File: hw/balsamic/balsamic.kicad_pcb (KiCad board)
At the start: 2 copper layers, 18.7 x 14.5 mm, 45 parts, among them J1 Conn_01x24, J2 AXT524124, J3 USB_B_Mini, SW1 SW_Push, U1 ISP1807-LR-RS, U2 BMI160, U4 MAX77658AANX+

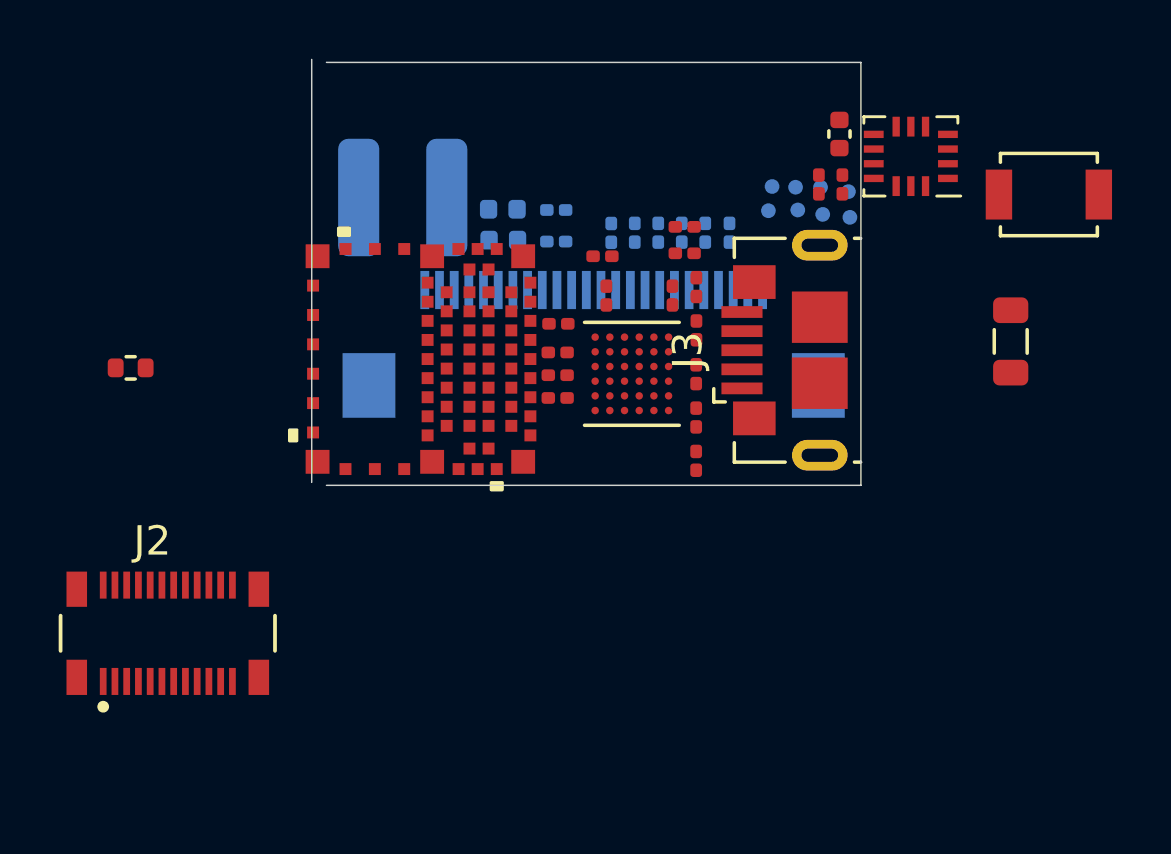
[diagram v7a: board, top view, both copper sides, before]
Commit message: Got board size to 16.1x9.825mm
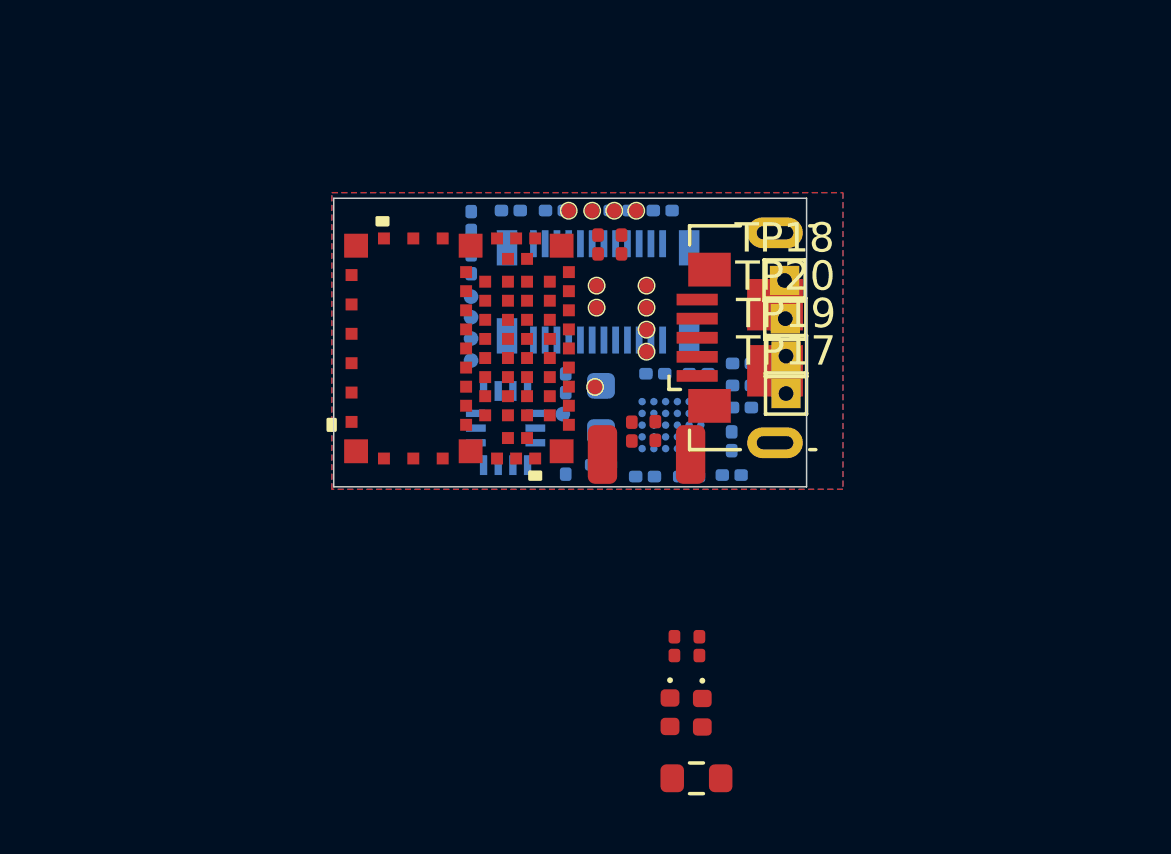
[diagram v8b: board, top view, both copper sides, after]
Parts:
- removed C16, C36: 22uF, Capacitor_SMD:C_0201_0603Metric
- removed C23, C28, C53: 1uF, Capacitor_SMD:C_0201_0603Metric
- removed C34: 10nF, Capacitor_SMD:C_0201_0603Metric
- removed C39: 0.47uF, Capacitor_SMD:C_0201_0603Metric
- removed C46: 100nF, Capacitor_SMD:C_0402_1005Metric
- removed J2: AXT524124, footprints:PANASONIC_AXT524124
- removed L1: 1.5uH, Inductor_SMD:L_0805_2012Metric
- removed R10: 0, Resistor_SMD:R_0201_0603Metric
- removed R11, R12: 4.7K, Resistor_SMD:R_0201_0603Metric
- removed R35: 0, Resistor_SMD:R_0402_1005Metric
- removed R9: 100k, Resistor_SMD:R_0201_0603Metric
- removed U4: MAX77658AANX+, footprints:MAX77658AANX&plus_
- added C1: 22uF, Capacitor_SMD:C_0201_0603Metric, B.Cu at (76.5, 68.6)
- added C11: 10uF, Capacitor_SMD:C_0201_0603Metric, B.Cu at (73.2, 71.7)
- added C12: 100nf, Capacitor_SMD:C_0201_0603Metric, B.Cu at (68.6, 62.6)
- added C2: 4.7uF, Capacitor_SMD:C_0201_0603Metric, B.Cu at (76.1, 71.7)
- added C3: 3300pF, Capacitor_SMD:C_0201_0603Metric, B.Cu at (71.7, 71.3)
- added C5: 1uF, Capacitor_SMD:C_0201_0603Metric, B.Cu at (75.0, 68.2)
- added C6: 10uF, Capacitor_SMD:C_0201_0603Metric, B.Cu at (70.1, 62.6)
- added C8: 10uF, Capacitor_SMD:C_0201_0603Metric, B.Cu at (76.5, 67.8)
- added C9: 1uF, Capacitor_SMD:C_0201_0603Metric, B.Cu at (76.1, 70.5)
- added L2: 1.5uH, Inductor_SMD:L_0603_1608Metric, B.Cu at (71.7, 69.4)
- added R1: 10K, Resistor_SMD:R_0201_0603Metric, F.Cu at (73.5, 70.2)
- added R2: 10K, Resistor_SMD:R_0201_0603Metric, F.Cu at (72.7, 70.2)
- added TP1: TestPoint, custom_testpoints:TestPoint_Pad_D0.5mm, B.Cu at (70.3, 69.6)
- added TP10: TestPoint, custom_testpoints:TestPoint_Pad_D0.5mm, F.Cu at (71.5, 65.2)
- added TP11: TestPoint, custom_testpoints:TestPoint_Pad_D0.5mm, F.Cu at (70.5, 62.6)
- added TP12: TestPoint, custom_testpoints:TestPoint_Pad_D0.5mm, F.Cu at (71.3, 62.6)
- added TP13: TestPoint, custom_testpoints:TestPoint_Pad_D0.5mm, F.Cu at (72.1, 62.6)
- added TP2: TestPoint, custom_testpoints:TestPoint_Pad_D0.5mm, F.Cu at (73.2, 67.5)
- added TP3: TestPoint, custom_testpoints:TestPoint_Pad_D0.5mm, B.Cu at (67.2, 67.0)
- added TP4: TestPoint, custom_testpoints:TestPoint_Pad_D0.5mm, B.Cu at (67.2, 66.3)
- added TP6: TestPoint, custom_testpoints:TestPoint_Pad_D0.5mm, B.Cu at (67.2, 65.6)
- added TP7: TestPoint, custom_testpoints:TestPoint_Pad_D0.5mm, F.Cu at (71.5, 68.7)
- added TP8: TestPoint, custom_testpoints:TestPoint_Pad_D0.5mm, F.Cu at (73.2, 65.2)
- added TP9: TestPoint, custom_testpoints:TestPoint_Pad_D0.5mm, F.Cu at (71.5, 66.0)
- added U3: MAX77651BEWVA+T, footprints:MAX77651BEWVA&plus_T, B.Cu at (74.0, 70.0)
- BT1, D1, D2, R15, R16, TP14, TP15, TP16: moved to F.Cu
- C10: value 22uF -> 10uF; moved to B.Cu
- C4: value 22uF -> 4.7uF; moved to B.Cu
- C45, R20, U2: moved to B.Cu
- C47: value 22uF -> 10uF
- C48: value 10uF -> 100nF
- C7: value 4.7uF -> 22uF; moved to B.Cu
- J1: value Conn_01x24 -> AXT524124; footprint Connector_FFC-FPC:Hirose_FH12-24S-0.5SH_1x24-1MP_P0.50mm_Horizontal -> footprints:PANASONIC_AXT524124
- R33, R34: value 220 -> 200; moved to F.Cu
- SW1: footprint Button_Switch_SMD:SW_SPST_B3U-1000P -> Resistor_SMD:R_0603_1608Metric
- TP17, TP18, TP19, TP20: footprint custom_testpoints:TestPoint_Pad_D0.5mm -> custom_testpoints:TestPoint_THTPad_1.0x1.0mm_Drill0.5mm; moved to F.Cu
- moved SW1 23.2 mm to (74.9, 82.0)
- moved D2 18.0 mm to (74.0, 79.7), turned to -90 degrees
- moved D1 17.5 mm to (75.1, 79.7), turned to -90 degrees
- moved U2 16.6 mm to (68.4, 70.0), turned to -90 degrees
- moved R34 15.4 mm to (74.2, 77.5), turned to -90 degrees
- moved R33 14.6 mm to (75.0, 77.5), turned to 90 degrees
- moved R20 13.4 mm to (70.5, 71.3), turned to -90 degrees
- moved TP5 13.3 mm to (67.2, 67.8)
- moved BT1 12.2 mm to (71.9, 71.0)
- moved C45 11.0 mm to (70.5, 68.5)
- moved C4 8.50 mm to (74.7, 71.7)
- moved TP16 7.93 mm to (73.2, 66.0), turned to 0 degrees
- moved TP14 7.28 mm to (72.8, 62.6), turned to 0 degrees
- moved TP15 7.02 mm to (73.2, 66.7), turned to 0 degrees
- moved C7 6.28 mm to (76.5, 69.3), turned to 0 degrees
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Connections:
- BT1 pad 1: Net-(BT1-Pad1) -> BATT
- BT1 pad 2: PGND -> GND
- C10 pad 1: LDO_1 -> PMU_LDO
- C10 pad 2: PGND -> GND
- C4 pad 1: SBB2_0.9V -> BATT
- C4 pad 2: PGND -> GND
- C45 pad 1: PGND -> GND
- C45 pad 2: VDD_nRF -> nRF_P1_06
- C47 pad 1: LDO_0 -> PMU_LDO
- C48 pad 2: LDO_0 -> PMU_LDO
- C49 pad 1: LDO_1 -> PMU_VSBB0
- C49 pad 2: PGND -> GND
- C50 pad 1: PGND -> GND
- C50 pad 2: LDO_1 -> PMU_VSBB0
- C7 pad 1: VBUS_USB -> PMU_VSYS
- C7 pad 2: PGND -> GND
- D1 pad 2: LDO_0 -> PMU_VSBB1
- D2 pad 2: LDO_0 -> PMU_VSBB1
- J1 pad 1: unconnected-(J1-Pad1) -> PMU_VSBB0
- J1 pad 10: LDO_1 -> DVP_D0
- J1 pad 11: LDO_1 -> DVP_SCL
- J1 pad 12: DVP_D7 -> DVP_D1
- J1 pad 13: DVP_XCLK -> DVP_LVLD
- J1 pad 14: DVP_D6 -> DVP_D2
- J1 pad 15: PGND -> DVP_FVLD
- J1 pad 16: DVP_D5 -> DVP_D3
- J1 pad 17: DVP_PCLK -> DVP_TRIG
- J1 pad 19: DVP_D0 -> GND
- J1 pad 2: GNDA -> GND
- J1 pad 20: DVP_D3 -> DVP_D5
- J1 pad 21: DVP_D1 -> PMU_LDO
- J1 pad 22: DVP_D2 -> DVP_D6
- J1 pad 23: SBB1_3.3V -> GNDA
- J1 pad 24: PGND -> DVP_D7
- J1 pad 3: DVP_SDA -> PMU_VSBB1
- J1 pad 4: LDO_0 -> DVP_MCLK
- J1 pad 5: DVP_SCL -> GND
- J1 pad 6: DVP_RST -> GND
- J1 pad 7: DVP_VSYNC -> DVP_INT
- J1 pad 8: DVP_PWDN -> DVP_PCLK
- J1 pad 9: DVP_HSYNC -> DVP_SDA
- J3 pad 4: nRF_UART_TX_DBUG -> unconnected-(J3-Pad4)
- J3 pad 5: PGND -> GND
- J3 pad 6: PGND -> GND
- R15 pad 1: LDO_1 -> PMU_VSBB1
- R16 pad 2: LDO_1 -> PMU_VSBB1
- R20 pad 1: LDO_1 -> PMU_VSBB1
- R20 pad 2: VDD_nRF -> nRF_P1_06
- SW1 pad 2: PGND -> PMU_VSBB1
- TP14 pad 1: INT_2_IMU -> DVP_TRIG
- TP15 pad 1: INT_1_IMU -> DVP_D2
- TP16 pad 1: PMU_ALERT_PIN -> DVP_D1
- TP17 pad 1: SPI_MISO -> PMU_VSBB1
- TP18 pad 1: SPI_MOSI -> Button
- TP19 pad 1: SPI_CLK -> nRF_LED1
- TP20 pad 1: SPI_CS_IMU -> nRF_LED2
- TP5 pad 1: NIRQ -> IMU_CLK
- U1 pad 1: PGND -> GND
- U1 pad 11: unconnected-(U1-Pad11) -> DVP_D1
- U1 pad 13: nRF_RST -> unconnected-(U1-Pad13)
- U1 pad 14: PGND -> GND
- U1 pad 15: unconnected-(U1-Pad15) -> DVP_D0
- U1 pad 16: PGND -> GND
- U1 pad 17: unconnected-(U1-Pad17) -> DVP_D2
- U1 pad 18: PGND -> GND
- U1 pad 19: unconnected-(U1-Pad19) -> IMU_MISO
- U1 pad 2: unconnected-(U1-Pad2) -> DVP_INT
- U1 pad 20: PGND -> GND
- U1 pad 21: PGND -> GND
- U1 pad 22: PGND -> GND
- U1 pad 23: PGND -> GND
- U1 pad 24: PGND -> GND
- U1 pad 25: PGND -> GND
- U1 pad 26: LDO_1 -> PMU_VSBB1
- U1 pad 27: unconnected-(U1-Pad27) -> IMU_CLK
- U1 pad 29: unconnected-(U1-Pad29) -> IMU_CS
- U1 pad 3: unconnected-(U1-Pad3) -> DVP_SDA
- U1 pad 31: PGND -> GND
- U1 pad 32: SPI_CLK -> nRF_LED1
- U1 pad 33: SPI_CS_IMU -> Button
- U1 pad 34: SPI_MOSI -> nRF_LED2
- U1 pad 35: SPI_MISO -> nRF_P0_05
- U1 pad 37: nRF_UART_RX -> unconnected-(U1-Pad37)
- U1 pad 38: unconnected-(U1-Pad38) -> nRF_P0_03
- U1 pad 39: Button -> unconnected-(U1-Pad39)
- U1 pad 40: unconnected-(U1-Pad40) -> nRF_P0_02
- U1 pad 41: nRF_UART_RX_DBUG -> DVP_TRIG
- U1 pad 42: unconnected-(U1-Pad42) -> nRF_P0_31
- U1 pad 43: nRF_UART_TX_DBUG -> unconnected-(U1-Pad43)
- U1 pad 44: unconnected-(U1-Pad44) -> nRF_P0_30
- U1 pad 45: unconnected-(U1-Pad45) -> DVP_PCLK
- U1 pad 46: unconnected-(U1-Pad46) -> DVP_FVLD
- U1 pad 47: unconnected-(U1-Pad47) -> DVP_D3
- U1 pad 48: unconnected-(U1-Pad48) -> DVP_LVLD
- U1 pad 49: unconnected-(U1-Pad49) -> IMU_INT2
- U1 pad 50: unconnected-(U1-Pad50) -> nRF_P1_06
- U1 pad 51: unconnected-(U1-Pad51) -> IMU_INT1
- U1 pad 52: unconnected-(U1-Pad52) -> nRF_P1_14
- U1 pad 53: unconnected-(U1-Pad53) -> nRF_P1_13
- U1 pad 54: unconnected-(U1-Pad54) -> PMU_GPIO_0
- U1 pad 55: VDD_nRF -> DVP_MCLK
- U1 pad 56: PMU_SCL -> DVP_SCL
- U1 pad 58: nRF_LED2 -> IMU_MOSI
- U1 pad 59: nRF_LED1 -> nRF_P1_12
- U1 pad 60: INT_2_IMU -> nRF_P1_10
- U1 pad 61: INT_1_IMU -> nRF_P1_11
- U1 pad 62: NIRQ -> PMU_NIRQ
- U1 pad 63: PMU_ALERT_PIN -> nRF_P1_04
- U1 pad 64: unconnected-(U1-Pad64) -> nRF_P1_01
- U1 pad 7: PGND -> GND
- U2 pad 1: SPI_MISO -> IMU_MISO
- U2 pad 12: SPI_CS_IMU -> IMU_CS
- U2 pad 13: SPI_CLK -> IMU_CLK
- U2 pad 14: SPI_MOSI -> IMU_MOSI
- U2 pad 4: INT_1_IMU -> IMU_INT1
- U2 pad 5: VDD_nRF -> nRF_P1_06
- U2 pad 6: PGND -> GND
- U2 pad 7: PGND -> GND
- U2 pad 8: VDD_nRF -> nRF_P1_06
- U2 pad 9: INT_2_IMU -> IMU_INT2
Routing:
- added copper zone on B.Cu, net GND
- added copper zone on F.Cu, net GND
- added copper zone on In1.Cu, net GND
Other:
- board size 18.7 x 14.5 mm -> 16.1 x 9.8 mm
- copper layers 2 -> 4
